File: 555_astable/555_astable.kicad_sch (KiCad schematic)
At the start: 11 parts, among them J1 Conn_01x02, J2 Conn_01x02, J3 Conn_01x02, SW1 SW_SPST, U1 NE555P

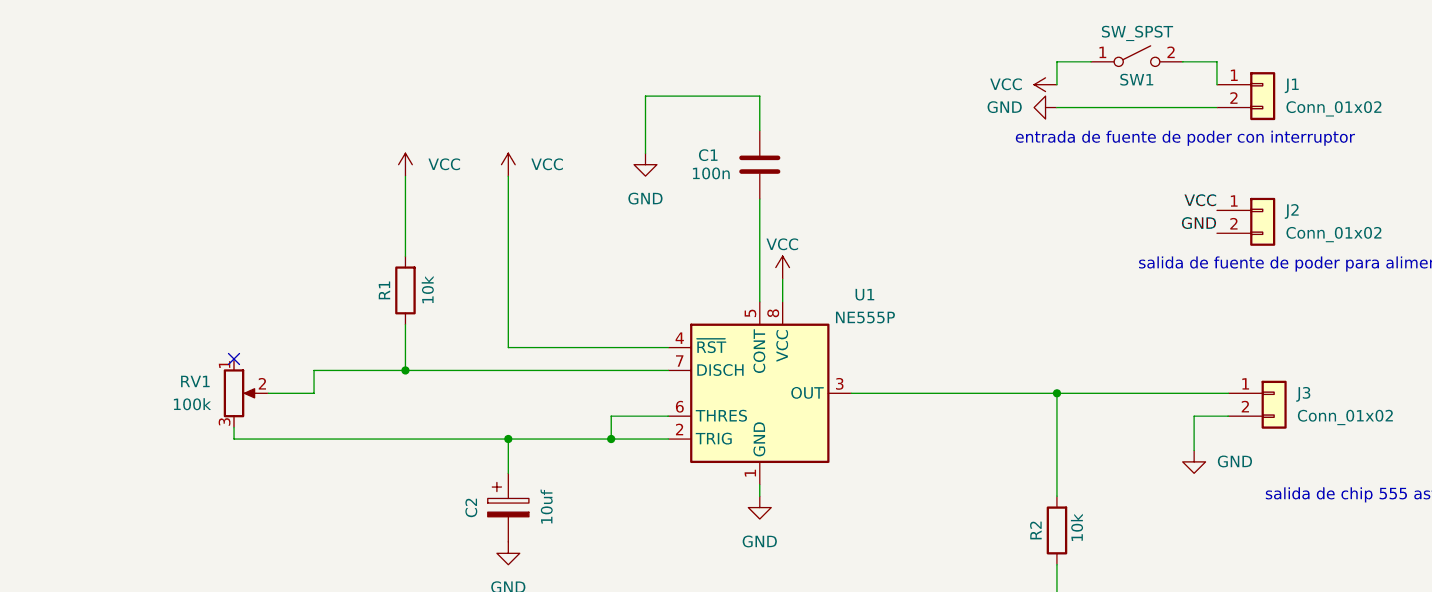
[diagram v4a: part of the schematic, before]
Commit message: nuevas footprints y pcb
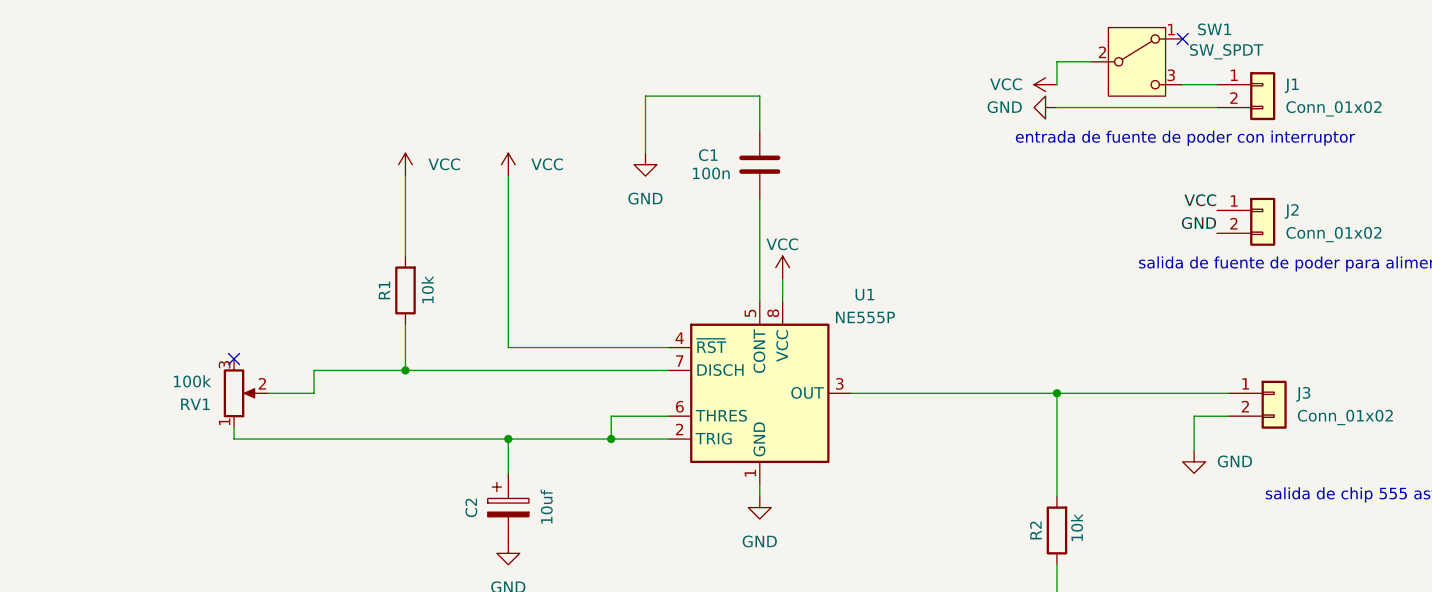
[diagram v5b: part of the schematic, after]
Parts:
- removed SW1: SW_SPST, Button_Switch_THT:SW_E-Switch_EG1271_SPDT, symbol Switch:SW_SPST
- added SW1: SW_SPDT, parla:spdt_ssd12d00g3, symbol Switch:SW_SPDT
- C2: footprint Capacitor_THT:C_Radial_D5.0mm_H5.0mm_P2.00mm -> Capacitor_THT:CP_Radial_D5.0mm_P2.50mm
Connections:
- net VCC: now also SW1.2 (B)
- net at RV1.1: now also C2.1, U1.2 (TRIG), U1.6 (THRES)
- net at J1.1 (Pin_1): now also SW1.3 (C)
- now unconnected: RV1.3
- no-connect marks 1 -> 2
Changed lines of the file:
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@@
 		(at 44.45 52.07)
 	)
+	(no_connect
+		(at 149.86 16.51)
+	)
 	(wire
 		(pts
@@
 	(wire
 		(pts
+			(xy 149.86 21.59) (xy 153.67 21.59)
+		)
+		(stroke
+			(width 0)
+			(type default)
+		)
+	)
+	(wire
+		(pts
 			(xy 135.89 19.05) (xy 135.89 21.59)
 		)
@@
 	(wire
 		(pts
-			(xy 153.67 19.05) (xy 153.67 21.59)
-		)
-		(stroke
-			(width 0)
-			(type default)
-		)
-	)
-	(wire
-		(pts
 			(xy 86.36 60.96) (xy 92.71 60.96)
 		)
@@
 		(pts
 			(xy 92.71 58.42) (xy 86.36 58.42)
-		)
-		(stroke
-			(width 0)
-			(type default)
-		)
-	)
-	(wire
-		(pts
-			(xy 149.86 19.05) (xy 153.67 19.05)
 		)
 		(stroke
@@
 		(lib_id "Device:R_Potentiometer")
 		(at 44.45 55.88 0)
+		(mirror x)
 		(unit 1)
 		(body_style 1)
@@
 		(in_pos_files yes)
 		(dnp no)
-		(fields_autoplaced yes)
 		(property "Reference" "RV1"
-			(at 41.91 54.6099 0)
+			(at 41.91 57.1501 0)
 			(show_name no)
 			(do_not_autoplace no)
@@
 		)
 		(property "Value" "100k"
-			(at 41.91 57.1499 0)
+			(at 41.91 54.6101 0)
 			(show_name no)
 			(do_not_autoplace no)
@@
 	)
 	(symbol
-		(lib_id "Switch:SW_SPST")
-		(at 144.78 19.05 0)
-		(unit 1)
-		(body_style 1)
-		(exclude_from_sim no)
-		(in_bom yes)
-		(on_board yes)
-		(in_pos_files yes)
-		(dnp no)
-		(property "Reference" "SW1"
-			(at 144.78 21.082 0)
-			(show_name no)
-			(do_not_autoplace no)
-			(effects
-				(font
-					(size 1.27 1.27)
-				)
-			)
-		)
-		(property "Value" "SW_SPST"
-			(at 144.78 15.748 0)
-			(show_name no)
-			(do_not_autoplace no)
-			(effects
-				(font
-					(size 1.27 1.27)
-				)
-			)
-		)
-		(property "Footprint" "Button_Switch_THT:SW_E-Switch_EG1271_SPDT"
-			(at 144.78 19.05 0)
-			(hide yes)
-			(show_name no)
-			(do_not_autoplace no)
-			(effects
-				(font
-					(size 1.27 1.27)
-				)
-			)
-		)
-		(property "Datasheet" ""
-			(at 144.78 19.05 0)
-			(hide yes)
-			(show_name no)
-			(do_not_autoplace no)
-			(effects
-				(font
-					(size 1.27 1.27)
-				)
-			)
-		)
-		(property "Description" "Single Pole Single Throw (SPST) switch"
-			(at 144.78 19.05 0)
-			(hide yes)
-			(show_name no)
-			(do_not_autoplace no)
-			(effects
-				(font
-					(size 1.27 1.27)
-				)
-			)
-		)
-		(pin "1"
-		)
-		(pin "2"
-		)
-		(instances
-			(project "555_astable"
-				(path "/f0997c31-ec15-4e60-aae3-7d657b633fbd"
-					(reference "SW1")
-					(unit 1)
-				)
-			)
-		)
-	)
-	(symbol
 		(lib_id "power:VCC")
 		(at 105.41 43.18 0)
@@
 			)
 		)
-		(property "Footprint" "Capacitor_THT:C_Radial_D5.0mm_H5.0mm_P2.00mm"
+		(property "Footprint" "Capacitor_THT:CP_Radial_D5.0mm_P2.50mm"
 			(at 75.8952 72.39 0)
 			(hide yes)
@@
 					(unit 1)
 				)
+			)
+		)
+	)
+	(symbol
+		(lib_id "Switch:SW_SPDT")
+		(at 144.78 19.05 0)
+		(unit 1)
+		(body_style 1)
+		(exclude_from_sim no)
+		(in_bom yes)
+		(on_board yes)
+		(in_pos_files yes)
+		(dnp no)
+		(property "Reference" "SW1"
+			(at 153.416 15.494 0)
+			(show_name no)
+			(do_not_autoplace no)
+			(effects
+				(font
+					(size 1.27 1.27)
+				)
+			)
+		)
+		(property "Value" "SW_SPDT"
+			(at 154.686 17.78 0)
+			(show_name no)
+			(do_not_autoplace no)
+			(effects
+				(font
+					(size 1.27 1.27)
+				)
+			)
+		)
+		(property "Footprint" "parla:spdt_ssd12d00g3"
+			(at 144.78 19.05 0)
+			(hide yes)
+			(show_name no)
+			(do_not_autoplace no)
+			(effects
+				(font
+					(size 1.27 1.27)
+				)
+			)
+		)
+		(property "Datasheet" ""
+			(at 144.78 26.67 0)
+			(hide yes)
+			(show_name no)
+			(do_not_autoplace no)
+			(effects
+				(font
+					(size 1.27 1.27)
+				)
+			)
+		)
+		(property "Description" "Switch, single pole double throw"
+			(at 144.78 19.05 0)
+			(hide yes)
+			(show_name no)
+			(do_not_autoplace no)
+			(effects
+				(font
+					(size 1.27 1.27)
+				)
+			)
+		)
+		(pin "3"
+		)
+		(pin "2"
+		)
+		(pin "1"
+		)
+		(instances
+			(project "555_astable"
+				(path "/f0997c31-ec15-4e60-aae3-7d657b633fbd"
+					(reference "SW1")
+					(unit 1)
+				)
